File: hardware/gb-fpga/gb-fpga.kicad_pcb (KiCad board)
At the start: 4 copper layers, 80.1 x 78.6 mm, 3 parts, among them U1 FPGA, U2 Flash

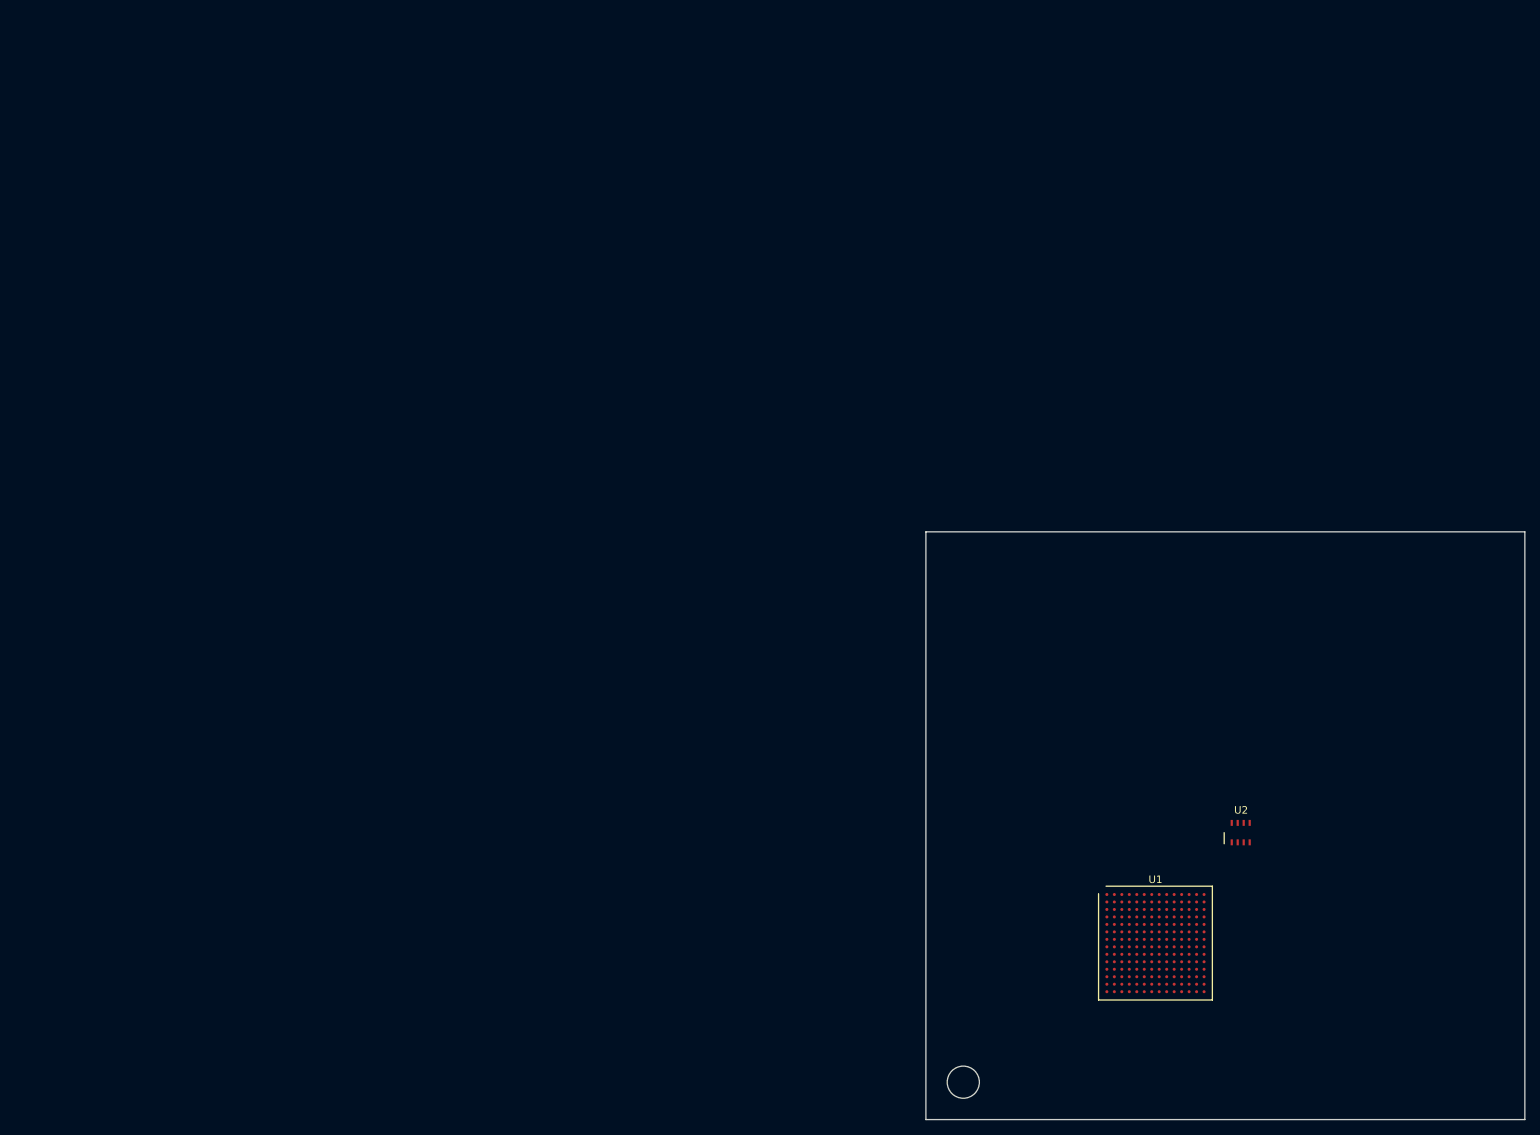
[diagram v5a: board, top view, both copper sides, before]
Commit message: Move board origin to 0 0
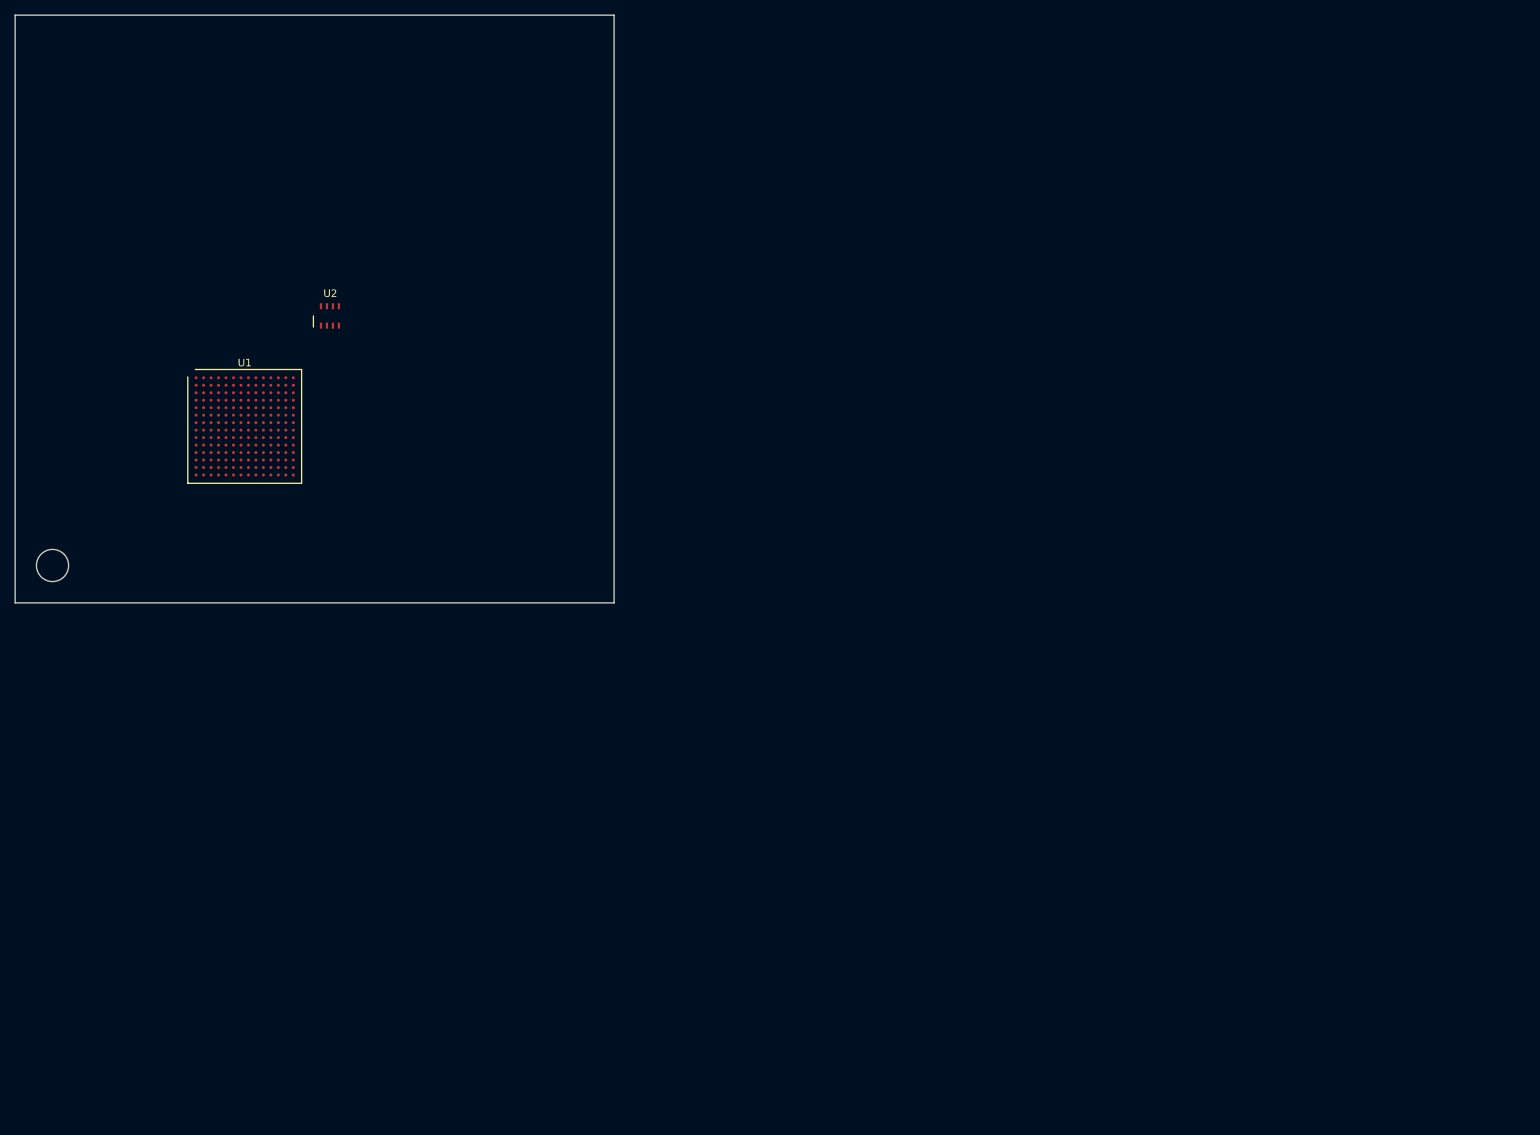
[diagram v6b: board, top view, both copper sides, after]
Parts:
- moved U2 140.0 mm to (42.1, -38.4)
- moved REF** 140.0 mm to (5.00, -5.00)
- moved U1 140.0 mm to (30.7, -23.6)
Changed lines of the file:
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@@
     (pad_drill 0.762)
     (pad_to_mask_clearance 0)
-    (aux_axis_origin 121.8 69.1)
+    (aux_axis_origin 0 0)
     (visible_elements FEFFFF7F)
     (pcbplotparams
@@
   )
   (module MountingHole:MountingHole_4.3mm_M4_DIN965 (layer F.Cu)
-    (at 126.8 64.1)
+    (at 5 -5)
     (descr "Mounting Hole 4.3mm, no annular, M4, DIN965")
     (tags "mounting hole 4.3mm no annular m4 din965")
@@
       (effects (font (size 1 1) (thickness 0.15)))
     )
+    (fp_circle (center 0 0) (end 4 0) (layer F.CrtYd) (width 0.05))
+    (fp_circle (center 0 0) (end 3.75 0) (layer Cmts.User) (width 0.15))
     (fp_text user %R (at 0.3 0) (layer F.Fab) hide
       (effects (font (size 1 1) (thickness 0.15)))
     )
-    (fp_circle (center 0 0) (end 3.75 0) (layer Cmts.User) (width 0.15))
-    (fp_circle (center 0 0) (end 4 0) (layer F.CrtYd) (width 0.05))
     (pad 1 np_thru_hole circle (at 0 0) (size 4.3 4.3) (drill 4.3) (layers *.Cu *.Mask))
   )
   (module Package_BGA:Xilinx_FTGB196 (layer F.Cu)
-    (at 152.5 45.5)
+    (at 30.7 -23.6)
     (descr "Spartan-7 BGA, 14x14 grid, 15x15mm package, 1mm pitch; https://www.xilinx.com/support/documentation/user_guides/ug475_7Series_Pkg_Pinout.pdf#page=261, NSMD pad definition Appendix A")
     (tags "BGA 196 1 FTGB196")
@@
       (effects (font (size 1 1) (thickness 0.15)))
     )
+    (fp_line (start -7.61 7.61) (end -7.61 -6.61) (layer F.SilkS) (width 0.12))
+    (fp_line (start 7.61 7.61) (end -7.61 7.61) (layer F.SilkS) (width 0.12))
+    (fp_line (start 7.61 -7.61) (end 7.61 7.61) (layer F.SilkS) (width 0.12))
+    (fp_line (start -6.61 -7.61) (end 7.61 -7.61) (layer F.SilkS) (width 0.12))
+    (fp_line (start 8.5 -8.5) (end -8.5 -8.5) (layer F.CrtYd) (width 0.05))
+    (fp_line (start 8.5 8.5) (end 8.5 -8.5) (layer F.CrtYd) (width 0.05))
+    (fp_line (start -8.5 8.5) (end 8.5 8.5) (layer F.CrtYd) (width 0.05))
+    (fp_line (start -8.5 -8.5) (end -8.5 8.5) (layer F.CrtYd) (width 0.05))
+    (fp_line (start 7.5 -7.5) (end 7.5 7.5) (layer F.Fab) (width 0.1))
+    (fp_line (start -6.5 -7.5) (end 7.5 -7.5) (layer F.Fab) (width 0.1))
+    (fp_line (start -7.5 -6.5) (end -6.5 -7.5) (layer F.Fab) (width 0.1))
+    (fp_line (start -7.5 7.5) (end -7.5 -6.5) (layer F.Fab) (width 0.1))
     (fp_line (start 7.5 7.5) (end -7.5 7.5) (layer F.Fab) (width 0.1))
-    (fp_line (start -7.5 7.5) (end -7.5 -6.5) (layer F.Fab) (width 0.1))
-    (fp_line (start -7.5 -6.5) (end -6.5 -7.5) (layer F.Fab) (width 0.1))
-    (fp_line (start -6.5 -7.5) (end 7.5 -7.5) (layer F.Fab) (width 0.1))
-    (fp_line (start 7.5 -7.5) (end 7.5 7.5) (layer F.Fab) (width 0.1))
-    (fp_line (start -8.5 -8.5) (end -8.5 8.5) (layer F.CrtYd) (width 0.05))
-    (fp_line (start -8.5 8.5) (end 8.5 8.5) (layer F.CrtYd) (width 0.05))
-    (fp_line (start 8.5 8.5) (end 8.5 -8.5) (layer F.CrtYd) (width 0.05))
-    (fp_line (start 8.5 -8.5) (end -8.5 -8.5) (layer F.CrtYd) (width 0.05))
-    (fp_line (start -6.61 -7.61) (end 7.61 -7.61) (layer F.SilkS) (width 0.12))
-    (fp_line (start 7.61 -7.61) (end 7.61 7.61) (layer F.SilkS) (width 0.12))
-    (fp_line (start 7.61 7.61) (end -7.61 7.61) (layer F.SilkS) (width 0.12))
-    (fp_line (start -7.61 7.61) (end -7.61 -6.61) (layer F.SilkS) (width 0.12))
     (fp_text user %R (at 0 0) (layer F.Fab)
       (effects (font (size 1 1) (thickness 0.15)))
@@
   )
   (module Package_SON:USON-8_4.0x3.0mm_P0.8mm (layer F.Cu)
-    (at 163.9 30.725)
+    (at 42.1 -38.375)
     (fp_text reference U2 (at 0.05 -3) (layer F.SilkS)
       (effects (font (size 1 1) (thickness 0.15)))
@@
       (effects (font (size 1 1) (thickness 0.15)))
     )
+    (fp_line (start 2.39 1.98) (end 2.39 -1.99) (layer F.CrtYd) (width 0.12))
+    (fp_line (start -2.37 1.98) (end 2.39 1.98) (layer F.CrtYd) (width 0.12))
+    (fp_line (start -2.37 -1.99) (end -2.37 1.98) (layer F.CrtYd) (width 0.12))
+    (fp_line (start 2.39 -1.99) (end -2.37 -1.99) (layer F.CrtYd) (width 0.12))
+    (fp_line (start -2 -1.5) (end 2 -1.5) (layer F.Fab) (width 0.12))
+    (fp_line (start 2 -1.5) (end 2 1.5) (layer F.Fab) (width 0.12))
+    (fp_line (start 2 1.5) (end -2 1.5) (layer F.Fab) (width 0.12))
+    (fp_line (start -2 1.5) (end -2 -1.5) (layer F.Fab) (width 0.12))
     (fp_line (start -2.21 1.49) (end -2.21 0) (layer F.SilkS) (width 0.12))
-    (fp_line (start -2 1.5) (end -2 -1.5) (layer F.Fab) (width 0.12))
-    (fp_line (start 2 1.5) (end -2 1.5) (layer F.Fab) (width 0.12))
-    (fp_line (start 2 -1.5) (end 2 1.5) (layer F.Fab) (width 0.12))
-    (fp_line (start -2 -1.5) (end 2 -1.5) (layer F.Fab) (width 0.12))
-    (fp_line (start 2.39 -1.99) (end -2.37 -1.99) (layer F.CrtYd) (width 0.12))
-    (fp_line (start -2.37 -1.99) (end -2.37 1.98) (layer F.CrtYd) (width 0.12))
-    (fp_line (start -2.37 1.98) (end 2.39 1.98) (layer F.CrtYd) (width 0.12))
-    (fp_line (start 2.39 1.98) (end 2.39 -1.99) (layer F.CrtYd) (width 0.12))
     (pad 1 smd rect (at -1.2 1.3) (size 0.3 0.8) (layers F.Cu F.Paste F.Mask)
       (net 129 "Net-(U2-Pad1)"))
@@
       (net 134 "Net-(U2-Pad8)"))
   )
-  (gr_line (start 121.8 -9.5) (end 121.8 69.1) (layer Edge.Cuts) (width 0.05))
-  (gr_line (start 201.9 -9.5) (end 121.8 -9.5) (layer Edge.Cuts) (width 0.05))
-  (gr_line (start 201.9 69.1) (end 201.9 -9.5) (layer Edge.Cuts) (width 0.05))
-  (gr_line (start 121.8 69.1) (end 201.9 69.1) (layer Edge.Cuts) (width 0.05))
+  (gr_line (start 0 -78.6) (end 0 0) (layer Edge.Cuts) (width 0.05))
+  (gr_line (start 80.1 -78.6) (end 0 -78.6) (layer Edge.Cuts) (width 0.05))
+  (gr_line (start 80.1 0) (end 80.1 -78.6) (layer Edge.Cuts) (width 0.05))
+  (gr_line (start 0 0) (end 80.1 0) (layer Edge.Cuts) (width 0.05))
 )

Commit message: Add second mounting hole
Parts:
- added REF**: MountingHole_4.3mm_M4_DIN965, MountingHole:MountingHole_4.3mm_M4_DIN965, F.Cu at (75.1, -5.00)
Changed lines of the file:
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@@
     (tracks 0)
     (zones 0)
-    (modules 3)
+    (modules 4)
     (nets 135)
   )
@@
     (mod_text_size 1 0.8)
     (mod_text_width 0.15)
-    (pad_size 1.524 1.524)
-    (pad_drill 0.762)
+    (pad_size 5.3 4.3)
+    (pad_drill 5.3)
     (pad_to_mask_clearance 0)
     (aux_axis_origin 0 0)
@@
   )
   (module MountingHole:MountingHole_4.3mm_M4_DIN965 (layer F.Cu)
+    (at 75.1 -5)
+    (descr "Mounting Hole 4.3mm, no annular, M4, DIN965")
+    (tags "mounting hole 4.3mm no annular m4 din965")
+    (attr virtual)
+    (fp_text reference REF** (at 0 -4.75) (layer F.SilkS) hide
+      (effects (font (size 1 1) (thickness 0.15)))
+    )
+    (fp_text value MountingHole_4.3mm_M4_DIN965 (at 0 4.75) (layer F.Fab) hide
+      (effects (font (size 1 1) (thickness 0.15)))
+    )
+    (fp_text user %R (at 0.3 0) (layer F.Fab) hide
+      (effects (font (size 1 1) (thickness 0.15)))
+    )
+    (fp_circle (center 0 0) (end 3.75 0) (layer Cmts.User) (width 0.15))
+    (fp_circle (center 0 0) (end 4 0) (layer F.CrtYd) (width 0.05))
+    (pad "" np_thru_hole oval (at 0 0) (size 5.3 4.3) (drill oval 5.3 4.3) (layers *.Cu *.Mask))
+  )
+  (module MountingHole:MountingHole_4.3mm_M4_DIN965 (layer F.Cu)
     (at 5 -5)
     (descr "Mounting Hole 4.3mm, no annular, M4, DIN965")
@@
       (effects (font (size 1 1) (thickness 0.15)))
     )
+    (fp_circle (center 0 0) (end 3.75 0) (layer Cmts.User) (width 0.15))
     (fp_circle (center 0 0) (end 4 0) (layer F.CrtYd) (width 0.05))
-    (fp_circle (center 0 0) (end 3.75 0) (layer Cmts.User) (width 0.15))
     (fp_text user %R (at 0.3 0) (layer F.Fab) hide
       (effects (font (size 1 1) (thickness 0.15)))
     )
-    (pad 1 np_thru_hole circle (at 0 0) (size 4.3 4.3) (drill 4.3) (layers *.Cu *.Mask))
+    (pad "" np_thru_hole circle (at 0 0) (size 4.3 4.3) (drill 4.3) (layers *.Cu *.Mask))
   )
   (module Package_BGA:Xilinx_FTGB196 (layer F.Cu)
@@
       (effects (font (size 1 1) (thickness 0.15)))
     )
+    (fp_line (start 7.5 7.5) (end -7.5 7.5) (layer F.Fab) (width 0.1))
+    (fp_line (start -7.5 7.5) (end -7.5 -6.5) (layer F.Fab) (width 0.1))
+    (fp_line (start -7.5 -6.5) (end -6.5 -7.5) (layer F.Fab) (width 0.1))
+    (fp_line (start -6.5 -7.5) (end 7.5 -7.5) (layer F.Fab) (width 0.1))
+    (fp_line (start 7.5 -7.5) (end 7.5 7.5) (layer F.Fab) (width 0.1))
+    (fp_line (start -8.5 -8.5) (end -8.5 8.5) (layer F.CrtYd) (width 0.05))
+    (fp_line (start -8.5 8.5) (end 8.5 8.5) (layer F.CrtYd) (width 0.05))
+    (fp_line (start 8.5 8.5) (end 8.5 -8.5) (layer F.CrtYd) (width 0.05))
+    (fp_line (start 8.5 -8.5) (end -8.5 -8.5) (layer F.CrtYd) (width 0.05))
+    (fp_line (start -6.61 -7.61) (end 7.61 -7.61) (layer F.SilkS) (width 0.12))
+    (fp_line (start 7.61 -7.61) (end 7.61 7.61) (layer F.SilkS) (width 0.12))
+    (fp_line (start 7.61 7.61) (end -7.61 7.61) (layer F.SilkS) (width 0.12))
     (fp_line (start -7.61 7.61) (end -7.61 -6.61) (layer F.SilkS) (width 0.12))
-    (fp_line (start 7.61 7.61) (end -7.61 7.61) (layer F.SilkS) (width 0.12))
-    (fp_line (start 7.61 -7.61) (end 7.61 7.61) (layer F.SilkS) (width 0.12))
-    (fp_line (start -6.61 -7.61) (end 7.61 -7.61) (layer F.SilkS) (width 0.12))
-    (fp_line (start 8.5 -8.5) (end -8.5 -8.5) (layer F.CrtYd) (width 0.05))
-    (fp_line (start 8.5 8.5) (end 8.5 -8.5) (layer F.CrtYd) (width 0.05))
-    (fp_line (start -8.5 8.5) (end 8.5 8.5) (layer F.CrtYd) (width 0.05))
-    (fp_line (start -8.5 -8.5) (end -8.5 8.5) (layer F.CrtYd) (width 0.05))
-    (fp_line (start 7.5 -7.5) (end 7.5 7.5) (layer F.Fab) (width 0.1))
-    (fp_line (start -6.5 -7.5) (end 7.5 -7.5) (layer F.Fab) (width 0.1))
-    (fp_line (start -7.5 -6.5) (end -6.5 -7.5) (layer F.Fab) (width 0.1))
-    (fp_line (start -7.5 7.5) (end -7.5 -6.5) (layer F.Fab) (width 0.1))
-    (fp_line (start 7.5 7.5) (end -7.5 7.5) (layer F.Fab) (width 0.1))
     (fp_text user %R (at 0 0) (layer F.Fab)
       (effects (font (size 1 1) (thickness 0.15)))
@@
       (effects (font (size 1 1) (thickness 0.15)))
     )
+    (fp_line (start -2.21 1.49) (end -2.21 0) (layer F.SilkS) (width 0.12))
+    (fp_line (start -2 1.5) (end -2 -1.5) (layer F.Fab) (width 0.12))
+    (fp_line (start 2 1.5) (end -2 1.5) (layer F.Fab) (width 0.12))
+    (fp_line (start 2 -1.5) (end 2 1.5) (layer F.Fab) (width 0.12))
+    (fp_line (start -2 -1.5) (end 2 -1.5) (layer F.Fab) (width 0.12))
+    (fp_line (start 2.39 -1.99) (end -2.37 -1.99) (layer F.CrtYd) (width 0.12))
+    (fp_line (start -2.37 -1.99) (end -2.37 1.98) (layer F.CrtYd) (width 0.12))
+    (fp_line (start -2.37 1.98) (end 2.39 1.98) (layer F.CrtYd) (width 0.12))
     (fp_line (start 2.39 1.98) (end 2.39 -1.99) (layer F.CrtYd) (width 0.12))
-    (fp_line (start -2.37 1.98) (end 2.39 1.98) (layer F.CrtYd) (width 0.12))
-    (fp_line (start -2.37 -1.99) (end -2.37 1.98) (layer F.CrtYd) (width 0.12))
-    (fp_line (start 2.39 -1.99) (end -2.37 -1.99) (layer F.CrtYd) (width 0.12))
-    (fp_line (start -2 -1.5) (end 2 -1.5) (layer F.Fab) (width 0.12))
-    (fp_line (start 2 -1.5) (end 2 1.5) (layer F.Fab) (width 0.12))
-    (fp_line (start 2 1.5) (end -2 1.5) (layer F.Fab) (width 0.12))
-    (fp_line (start -2 1.5) (end -2 -1.5) (layer F.Fab) (width 0.12))
-    (fp_line (start -2.21 1.49) (end -2.21 0) (layer F.SilkS) (width 0.12))
     (pad 1 smd rect (at -1.2 1.3) (size 0.3 0.8) (layers F.Cu F.Paste F.Mask)
       (net 129 "Net-(U2-Pad1)"))

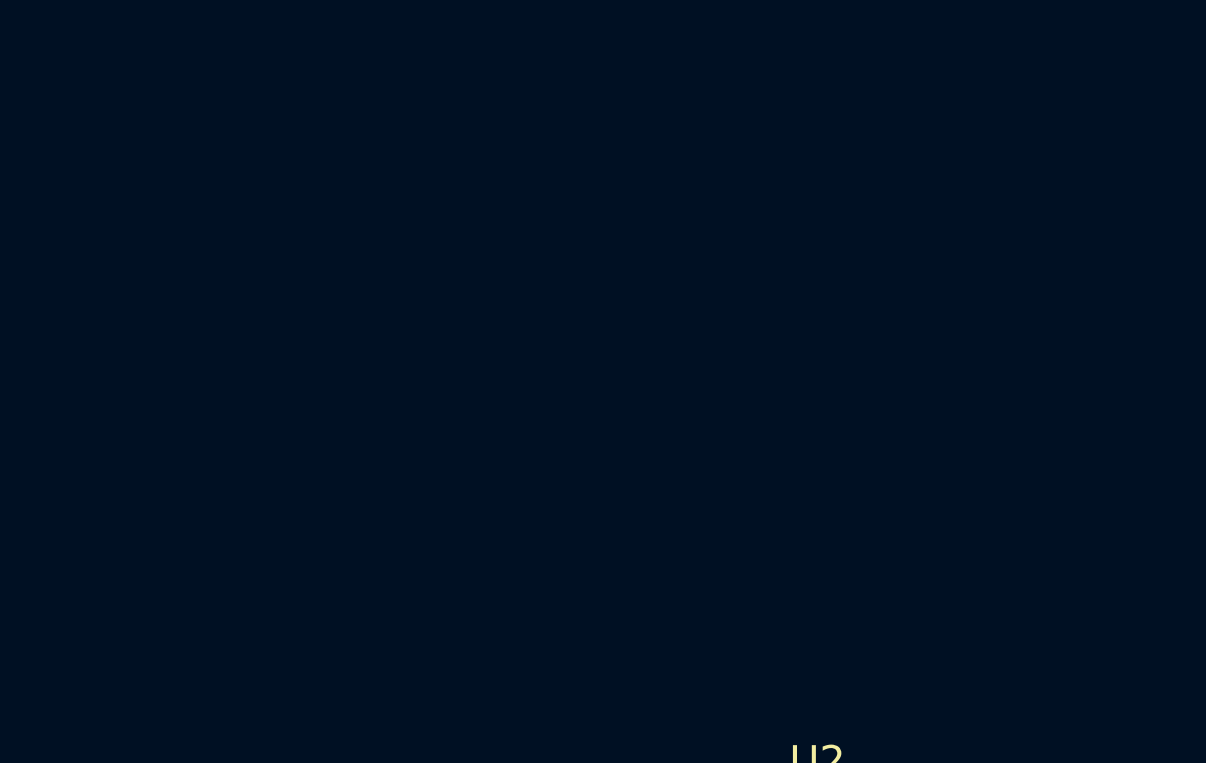
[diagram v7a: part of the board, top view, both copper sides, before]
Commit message: Add usb parts
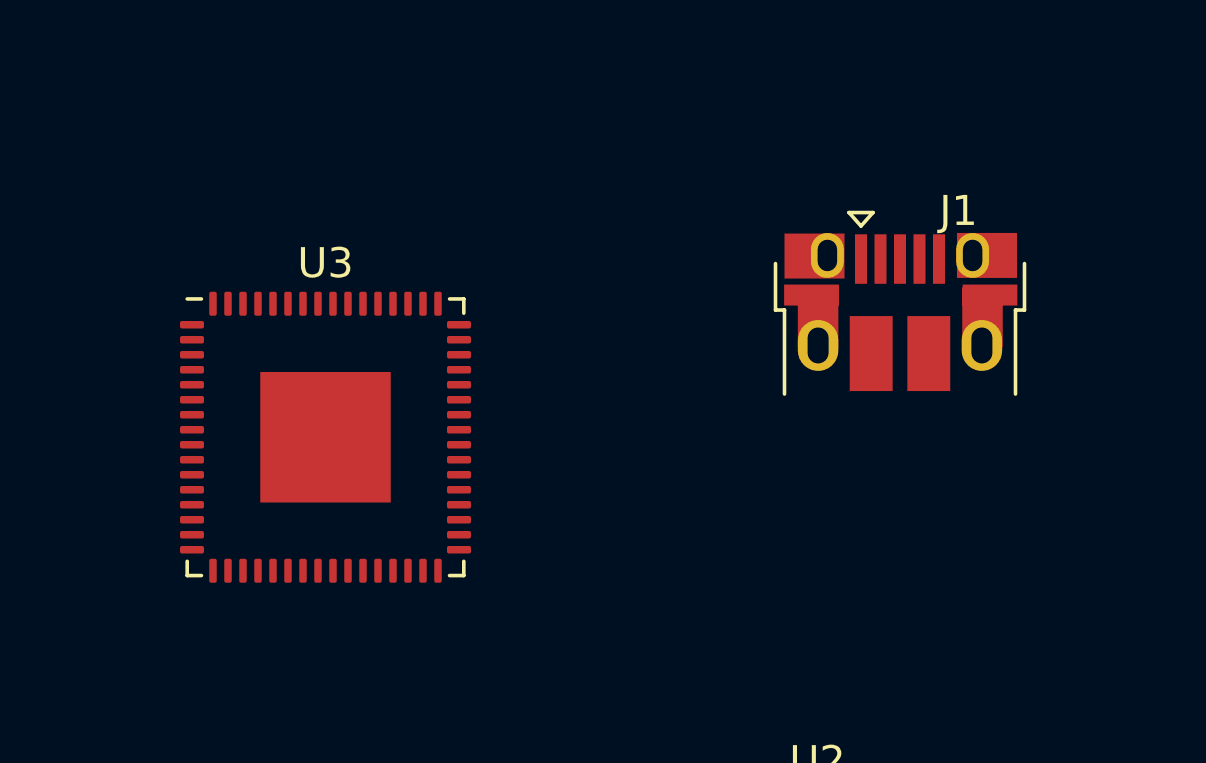
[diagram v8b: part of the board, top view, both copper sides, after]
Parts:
- added J1: USB_B_Micro, Connector_USB:USB_Micro-B_Amphenol_10103594-0001LF_Horizontal, F.Cu at (44.9, -56.4)
- added U3: FT2232HQ, Package_DFN_QFN:QFN-64-1EP_9x9mm_P0.5mm_EP4.35x4.35mm, F.Cu at (25.8, -52.2)
- U1: value FPGA -> xc7s25ftgb196
- U2: value Flash -> MX25R3235FZBxx1
